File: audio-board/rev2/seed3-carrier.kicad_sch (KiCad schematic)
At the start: 56 parts, among them J1 NRJ4HF, J2 SJ3-35063AG, J3 DISPLAY_UART, J4 SJ3-35063AG, J5 LINE_OUT, J6 POWER_BOARD, Q1 AO3401A, Q2 2N7002, U1 TLV9061IDBVR, U2 TPA6132A2RTE

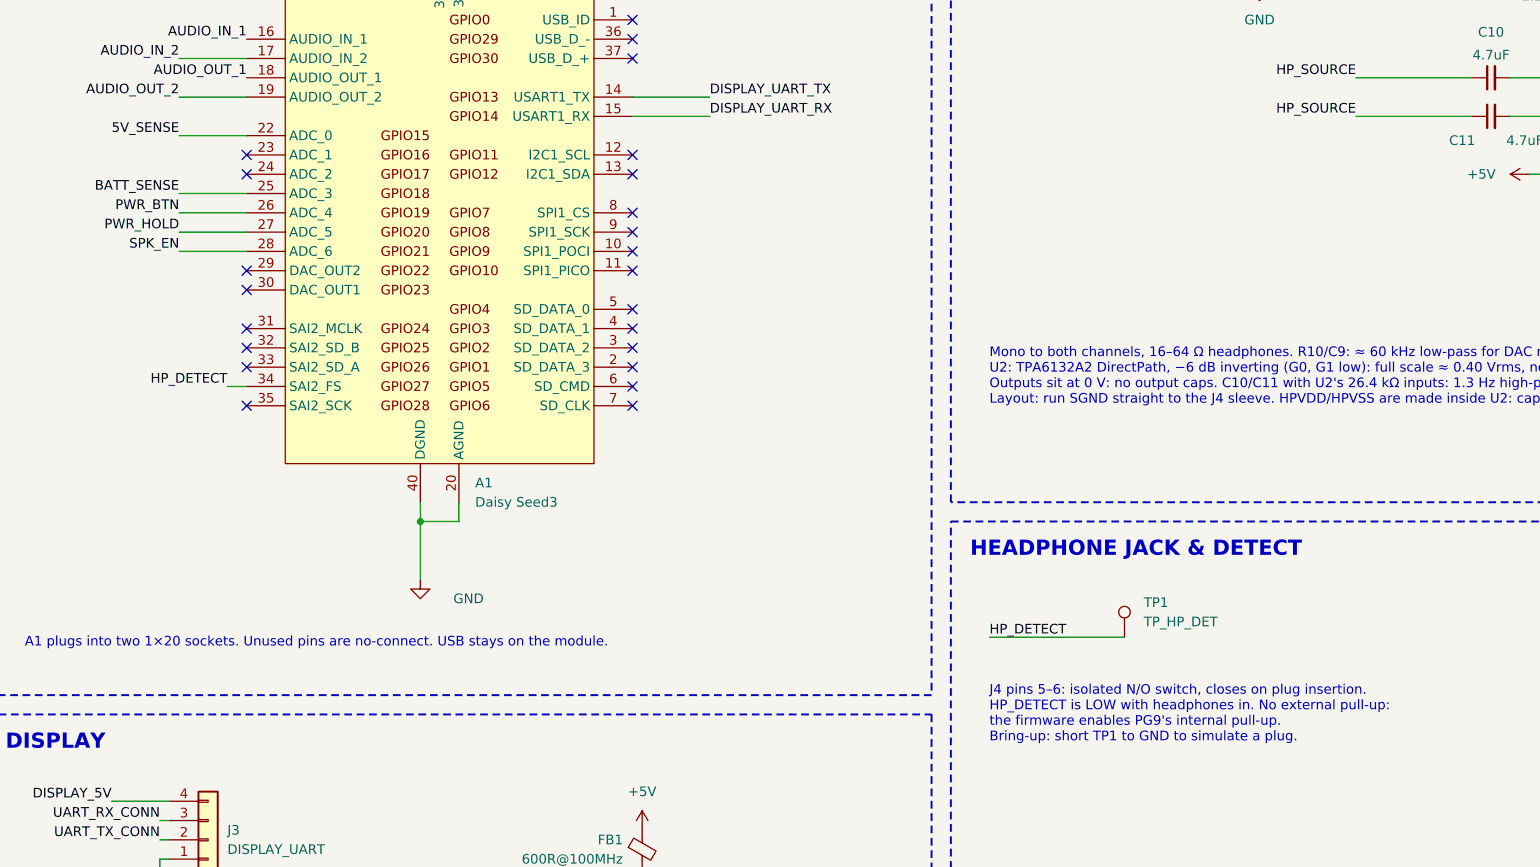
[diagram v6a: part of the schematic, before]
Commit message: Re-place the carrier passives and route the analog section
Each filter and divider now sits at its load, so long runs are the
low-impedance ones: the AUX sum moves under Daisy pin 17 (J2 moves right
so its lines no longer cross the guitar row), R10/C9 join U2's input caps,
and the VREF divider sits at R1. U2 is rotated 180 degrees so OUTL and SGND
run side by side on L1 to J4's tip and sleeve; OUTR takes one via to L4.
J5 moves into the power corner so the power board's ground loop through
J5/J6 stays away from U1 and U2.

Every SMD GND pad gets its own via. The guitar row, AUX and headphone
paths, speaker send, U1/U2 decoupling, power entry and an analog-only +5V
branch on L4 are routed. HP_DETECT moves from Daisy pin 34 to pin 23,
which sits above the headphone section. DRC is clean apart from the
existing jack-overhang silk warnings.

Co-Authored-By: Claude Opus 5.5 <noreply@anthropic.com>
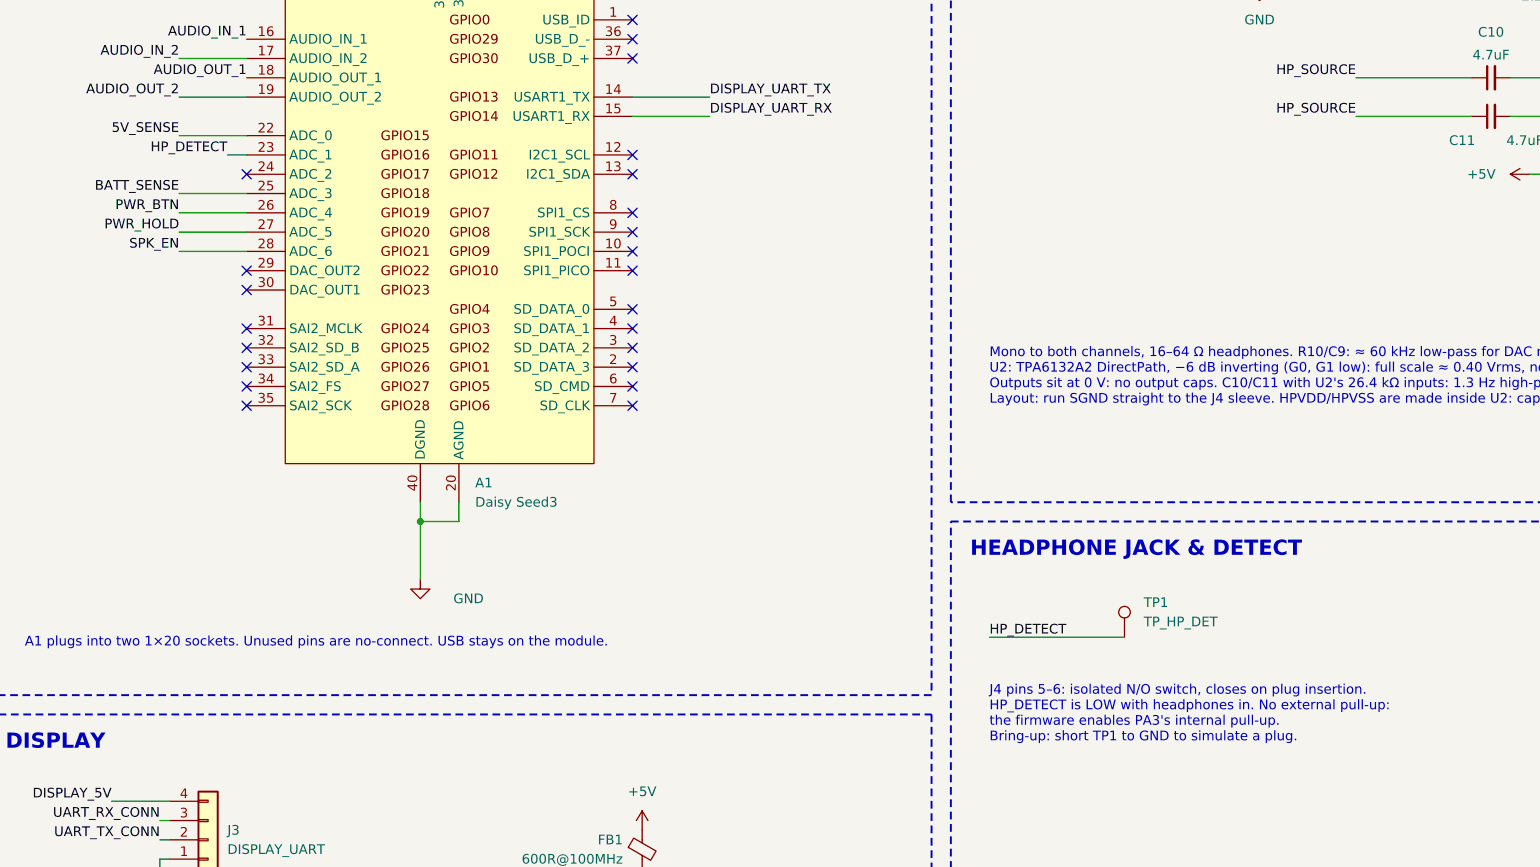
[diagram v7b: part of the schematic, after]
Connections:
- net HP_DETECT: now also A1.23 (ADC_1); no longer A1.34 (SAI2_FS)
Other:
- note added: "J4 pins 5–6: isolated N/O switch, closes on plug insertion. HP_DETECT is LOW with headphones in. No external pull-up: the firmware enables PA3's internal pull-up. Bring-up: short TP1 to GND to simulate a plug."
- note removed: "J4 pins 5–6: isolated N/O switch, closes on plug insertion. HP_DETECT is LOW with headphones in. No external pull-up: the firmware enables PG9's internal pull-up. Bring-up: short TP1 to GND to simulate a plug."
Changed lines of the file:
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@@
 	)
 	(no_connect
-		(at 173.99 66.04)
+		(at 173.99 96.52)
 	)
 	(wire
@@
 	(wire
 		(pts
-			(xy 171.45 96.52) (xy 173.99 96.52)
+			(xy 171.45 66.04) (xy 173.99 66.04)
 		)
 		(stroke
@@
 	)
 	(label "HP_DETECT"
-		(at 171.45 96.52 180)
+		(at 171.45 66.04 180)
 		(effects
 			(font
@@
 		)
 	)
-	(text "J4 pins 5–6: isolated N/O switch, closes on plug insertion.\nHP_DETECT is LOW with headphones in. No external pull-up:\nthe firmware enables PG9's internal pull-up.\nBring-up: short TP1 to GND to simulate a plug."
+	(text "J4 pins 5–6: isolated N/O switch, closes on plug insertion.\nHP_DETECT is LOW with headphones in. No external pull-up:\nthe firmware enables PA3's internal pull-up.\nBring-up: short TP1 to GND to simulate a plug."
 		(exclude_from_sim no)
 		(at 271.78 135.89 0)

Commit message: Use screw terminals for the power board, display and speaker connectors
J6 becomes a 4-way 3.5 mm screw terminal (5V, GND, BAT, MUTE) and J3 a
3-way (GND, TX, RX), side by side on the rear edge; J5 becomes a 2-way
(LINE+, LINE-) on the right edge. All three open toward the board edge and
have their terminal functions on the silkscreen. KF350-3.5 blocks from
LCSC; J6 is two 2-ways slid together.

The power button and PWR_HOLD move to the power board, so R14-R16 and C18
go and Daisy pins 26/27 become no-connects. The display is powered from the
power board, so FB1, C8 and DISPLAY_5V go. LINE- is LINE_REF, 1k to GND
through the new R21, to match R11's source impedance for the speaker amp's
differential input. R9 goes to 10k to match R8.

The parts under J6 and J3 are re-placed one column per terminal, and the
power entry, analog +5V branch start and speaker send are re-routed. ERC is
clean, the board check passes with no errors, and schematic parity holds.

Co-Authored-By: Claude Opus 5.5 <noreply@anthropic.com>
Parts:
- removed C18: 100nF, Capacitor_SMD:C_1206_3216Metric_Pad1.33x1.80mm_HandSolder, symbol Device:C_Small
- removed C8: 47uF 16V, Capacitor_SMD:C_1210_3225Metric_Pad1.33x2.70mm_HandSolder, symbol Device:C_Small
- removed FB1: 600R@100MHz, Inductor_SMD:L_1206_3216Metric_Pad1.22x1.90mm_HandSolder, symbol Device:FerriteBead_Small
- removed R14, R16: 1k, Resistor_SMD:R_1206_3216Metric_Pad1.30x1.75mm_HandSolder, symbol Device:R_Small_US
- removed R15: 100k, Resistor_SMD:R_1206_3216Metric_Pad1.30x1.75mm_HandSolder, symbol Device:R_Small_US
- added R21: 1k, Resistor_SMD:R_1206_3216Metric_Pad1.30x1.75mm_HandSolder, symbol Device:R_Small_US
- J3: footprint Connector_PinHeader_2.54mm:PinHeader_1x04_P2.54mm_Vertical -> TerminalBlock_Phoenix:TerminalBlock_Phoenix_PT-1,5-3-3.5-H_1x03_P3.50mm_Horizontal; symbol Connector_Generic:Conn_01x04 -> Connector_Generic:Conn_01x03; LCSC C53055674 -> C474893
- J5: value LINE_OUT -> SPEAKER_SEND; footprint Connector_JST:JST_XH_B2B-XH-A_1x02_P2.50mm_Vertical -> TerminalBlock_Phoenix:TerminalBlock_Phoenix_PT-1,5-2-3.5-H_1x02_P3.50mm_Horizontal; LCSC C158012 -> C474892
- J6: footprint Connector_JST:JST_XH_B8B-XH-A_1x08_P2.50mm_Vertical -> TerminalBlock_Phoenix:TerminalBlock_Phoenix_PT-1,5-4-3.5-H_1x04_P3.50mm_Horizontal; symbol Connector_Generic:Conn_01x08 -> Connector_Generic:Conn_01x04; LCSC C157972 -> C474892
- R9: value 1k -> 10k; LCSC C4410 -> C17902
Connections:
- net 5V_IN: no longer J6.2 (Pin_2)
- net BATT_SENSE_CONN: now also J6.3 (Pin_3); no longer J6.5 (Pin_5)
- net GND: now also J6.2 (Pin_2), R21.1; no longer J5.2 (Pin_2), J6.3 (Pin_3), J6.4 (Pin_4)
- net SPK_MUTE: now also J6.4 (Pin_4); no longer J6.8 (Pin_8)
- removed net DISPLAY_5V: J3.4 (Pin_4)
- net PWR_BTN: no longer names the net of A1.26 (ADC_4)
- removed net PWR_BTN_CONN: J6.6 (Pin_6)
- net PWR_HOLD: no longer names the net of A1.27 (ADC_5)
- removed net PWR_HOLD_CONN: J6.7 (Pin_7)
- new net LINE_REF: J5.2 (Pin_2), R21.2
- no-connect marks 28 -> 30
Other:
- note added: "AUDIO_OUT_2 drives J5 (speaker amp, differential input) directly. R11/C16: ≈ 48 kHz low-pass, 1k out. R12: DC return. J5: LINE+ = LINE_OUT, LINE− = LINE_REF. R21 matches R11's 1k so the amp's input sees equal source impedances. Wire LINE− to the amp's IN− only. Assumes pin 19 at 0 V DC (TEST_PLAN 5.16)."
- note added: "J3: 3-way screw terminal. The display takes its power from the power board, so only the UART and its GND come here. R8/R9 (10k each) limit current if a wire is swapped or the display and Daisy power up at different times. Keep the UART at 230400 baud or less."
- note added: "J6 goes to the power board: a 4-way 3.5 mm screw terminal (two KF350-3.5-2P slid together). Pin 3 (BATT_SENSE) must stay within 0–3.3 V: the power board's divider sets that. GND sits between 5V_IN and the signals, so a stray strand from 5V_IN can only reach GND. SPK_MUTE is open drain. The power board pulls it up, so the speaker amp stays muted unless SPK_EN is high. R13 limits current into an un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"
- note removed: "AUDIO_OUT_2 drives J5 (to the speaker amp) directly. R11/C16: ≈ 48 kHz low-pass, 1k out. R12: DC return. Assumes pin 19 sits at 0 V DC (TEST_PLAN 5.16). With headphones in, the firmware drives SPK_EN low."
- note removed: "J6 goes to the power board (JST-XH, 8 pins). Pins 5–7 are 3.3 V logic: nothing above 3.3 V on them. SPK_MUTE is open drain. The power board pulls it up, so the speaker amp stays muted unless SPK_EN is high. R13, R16 and R14 limit current into an unpowered Daisy. R15 holds PWR_HOLD low while the Daisy is absent or booting."
- note removed: "R8/R9 limit current if the cable is miswired or hot-plugged. R8 is 10k so the Daisy's TX can't power an unpowered display (Daisy on USB): keep the UART at 230400 baud or less. FB1/C8 keep the display's current pulses (Wi-Fi, backlight) off +5V."
